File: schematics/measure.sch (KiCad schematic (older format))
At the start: 7 parts

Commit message: split into 2 sheets + drc
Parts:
- gave numbers to parts that had none: 7
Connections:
- net at U3.1 (IN+): now also P6.2 (P2), U3.12 (VBUS), U3.2 (IN+), U3.3 (IN+)
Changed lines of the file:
@@
 $EndDescr
 $Comp
-L INA260 U?
+L INA260 U3
 U 1 1 5881C68E
 P 5550 4200
-F 0 "U?" H 5650 4100 60  0000 C CNN
+F 0 "U3" H 5650 4100 60  0000 C CNN
 F 1 "INA260" V 6000 4700 60  0000 C CNN
 F 2 "" H 5550 4200 60  0001 C CNN
@@
 $EndComp
 $Comp
-L R_Small R?
+L R_Small R4
 U 1 1 5881C6C5
 P 4950 3650
-F 0 "R?" V 4850 3600 50  0000 L CNN
+F 0 "R4" V 4850 3600 50  0000 L CNN
 F 1 "0R_NP" V 4950 3600 50  0000 L CNN
 F 2 "" H 4950 3650 50  0000 C CNN
@@
 $EndComp
 $Comp
-L R_Small R?
+L R_Small R5
 U 1 1 5881C6FE
 P 4950 3750
-F 0 "R?" V 5050 3700 50  0000 L CNN
+F 0 "R5" V 5050 3700 50  0000 L CNN
 F 1 "0R" V 4950 3700 50  0000 L CNN
 F 2 "" H 4950 3750 50  0000 C CNN
@@
 $EndComp
 $Comp
-L GND #PWR?
+L GND #PWR014
 U 1 1 5881C8A1
 P 4700 3750
-F 0 "#PWR?" H 4700 3500 50  0001 C CNN
+F 0 "#PWR014" H 4700 3500 50  0001 C CNN
 F 1 "GND" H 4700 3600 50  0000 C CNN
 F 2 "" H 4700 3750 50  0000 C CNN
@@
 $EndComp
 $Comp
-L +3.3V #PWR?
+L +3.3V #PWR015
 U 1 1 5881C8BE
 P 4700 3650
-F 0 "#PWR?" H 4700 3500 50  0001 C CNN
+F 0 "#PWR015" H 4700 3500 50  0001 C CNN
 F 1 "+3.3V" H 4700 3790 50  0000 C CNN
 F 2 "" H 4700 3650 50  0000 C CNN
@@
 	4700 3750 4850 3750
 $Comp
-L R_Small R?
+L R_Small R6
 U 1 1 5881C9C3
 P 4950 4150
-F 0 "R?" V 4850 4100 50  0000 L CNN
+F 0 "R6" V 4850 4100 50  0000 L CNN
 F 1 "0R_NP" V 4950 4100 50  0000 L CNN
 F 2 "" H 4950 4150 50  0000 C CNN
@@
 $EndComp
 $Comp
-L R_Small R?
+L R_Small R7
 U 1 1 5881C9C9
 P 4950 4250
-F 0 "R?" V 5050 4200 50  0000 L CNN
+F 0 "R7" V 5050 4200 50  0000 L CNN
 F 1 "0R" V 4950 4200 50  0000 L CNN
 F 2 "" H 4950 4250 50  0000 C CNN
@@
 	5150 4250 5050 4250
 $Comp
-L GND #PWR?
+L GND #PWR016
 U 1 1 5881C9D1
 P 4700 4250
-F 0 "#PWR?" H 4700 4000 50  0001 C CNN
+F 0 "#PWR016" H 4700 4000 50  0001 C CNN
 F 1 "GND" H 4700 4100 50  0000 C CNN
 F 2 "" H 4700 4250 50  0000 C CNN
@@
 $EndComp
 $Comp
-L +3.3V #PWR?
+L +3.3V #PWR017
 U 1 1 5881C9D7
 P 4700 4150
-F 0 "#PWR?" H 4700 4000 50  0001 C CNN
+F 0 "#PWR017" H 4700 4000 50  0001 C CNN
 F 1 "+3.3V" H 4700 4290 50  0000 C CNN
 F 2 "" H 4700 4150 50  0000 C CNN
@@
 	6700 4000 6700 4100
 $Comp
-L GND #PWR?
+L GND #PWR018
 U 1 1 5881CC9E
 P 6700 4100
-F 0 "#PWR?" H 6700 3850 50  0001 C CNN
+F 0 "#PWR018" H 6700 3850 50  0001 C CNN
 F 1 "GND" H 6700 3950 50  0000 C CNN
 F 2 "" H 6700 4100 50  0000 C CNN
@@
 	6700 3900 7150 3900
 $Comp
-L +3.3V #PWR?
+L +3.3V #PWR019
 U 1 1 5881CD56
 P 7700 3850
-F 0 "#PWR?" H 7700 3700 50  0001 C CNN
+F 0 "#PWR019" H 7700 3700 50  0001 C CNN
 F 1 "+3.3V" H 7700 3990 50  0000 C CNN
 F 2 "" H 7700 3850 50  0000 C CNN
@@
 Connection ~ 6950 3900
 $Comp
-L CONN_01X02 P?
+L CONN_01X02 P7
 U 1 1 5881CF01
 P 7250 3250
-F 0 "P?" H 7250 3400 50  0000 C CNN
+F 0 "P7" H 7250 3400 50  0000 C CNN
 F 1 "Power_OUT" V 7350 3250 50  0000 C CNN
 F 2 "" H 7250 3250 50  0000 C CNN
@@
 $EndComp
 $Comp
-L CONN_01X02 P?
+L CONN_01X02 P6
 U 1 1 5881CF96
 P 4700 3150
-F 0 "P?" H 4700 3300 50  0000 C CNN
+F 0 "P6" H 4700 3300 50  0000 C CNN
 F 1 "Power_IN" V 4800 3150 50  0000 C CNN
 F 2 "" H 4700 3150 50  0000 C CNN
@@
 	6700 3200 7050 3200
 $Comp
-L GND #PWR?
+L GND #PWR020
 U 1 1 5881D061
 P 7050 3300
-F 0 "#PWR?" H 7050 3050 50  0001 C CNN
+F 0 "#PWR020" H 7050 3050 50  0001 C CNN
 F 1 "GND" H 7050 3150 50  0000 C CNN
 F 2 "" H 7050 3300 50  0000 C CNN
@@
 	5350 3100 4900 3100
 $Comp
-L GND #PWR?
+L GND #PWR021
 U 1 1 5881D145
 P 4900 3200
-F 0 "#PWR?" H 4900 2950 50  0001 C CNN
+F 0 "#PWR021" H 4900 2950 50  0001 C CNN
 F 1 "GND" H 4900 3050 50  0000 C CNN
 F 2 "" H 4900 3200 50  0000 C CNN
@@
 Wire Wire Line
 	6950 3850 7700 3850
+Connection ~ 5350 3200
+Connection ~ 6700 3400
+Connection ~ 6700 3200
 $EndSCHEMATC

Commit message: added pullups for I2C and alert
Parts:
- added R13, R14, R15: 1K, Resistors_SMD:R_0805_HandSoldering, symbol R_Small
- P6, P7: footprint (none) -> Terminal_Blocks:TerminalBlock_Pheonix_MKDS1.5-2pol
- R10: renamed from R5; footprint (none) -> Resistors_SMD:R_0805_HandSoldering
- R11: renamed from R6; footprint (none) -> Resistors_SMD:R_0805_HandSoldering
- R12: renamed from R7; footprint (none) -> Resistors_SMD:R_0805_HandSoldering
- R9: renamed from R4; footprint (none) -> Resistors_SMD:R_0805_HandSoldering
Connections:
- net +3V3: now also R13.1
- net ALERT: now also R15.2
- net I2C_SCL: now also R14.2
- net I2C_SDA: now also R13.2, R14.1, R15.1
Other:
- moved on the sheet: P7
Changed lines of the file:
@@
 $EndComp
 $Comp
-L R_Small R4
+L R_Small R9
 U 1 1 5881C6C5
 P 4950 3650
-F 0 "R4" V 4850 3600 50  0000 L CNN
+F 0 "R9" V 4850 3600 50  0000 L CNN
 F 1 "0R_NP" V 4950 3600 50  0000 L CNN
-F 2 "" H 4950 3650 50  0000 C CNN
+F 2 "Resistors_SMD:R_0805_HandSoldering" H 4950 3650 50  0001 C CNN
 F 3 "" H 4950 3650 50  0000 C CNN
 	1    4950 3650
@@
 $EndComp
 $Comp
-L R_Small R5
+L R_Small R10
 U 1 1 5881C6FE
 P 4950 3750
-F 0 "R5" V 5050 3700 50  0000 L CNN
+F 0 "R10" V 5050 3700 50  0000 L CNN
 F 1 "0R" V 4950 3700 50  0000 L CNN
-F 2 "" H 4950 3750 50  0000 C CNN
+F 2 "Resistors_SMD:R_0805_HandSoldering" H 4950 3750 50  0001 C CNN
 F 3 "" H 4950 3750 50  0000 C CNN
 	1    4950 3750
@@
 	4700 3750 4850 3750
 $Comp
-L R_Small R6
+L R_Small R11
 U 1 1 5881C9C3
 P 4950 4150
-F 0 "R6" V 4850 4100 50  0000 L CNN
+F 0 "R11" V 4850 4100 50  0000 L CNN
 F 1 "0R_NP" V 4950 4100 50  0000 L CNN
-F 2 "" H 4950 4150 50  0000 C CNN
+F 2 "Resistors_SMD:R_0805_HandSoldering" H 4950 4150 50  0001 C CNN
 F 3 "" H 4950 4150 50  0000 C CNN
 	1    4950 4150
@@
 $EndComp
 $Comp
-L R_Small R7
+L R_Small R12
 U 1 1 5881C9C9
 P 4950 4250
-F 0 "R7" V 5050 4200 50  0000 L CNN
+F 0 "R12" V 5050 4200 50  0000 L CNN
 F 1 "0R" V 4950 4200 50  0000 L CNN
-F 2 "" H 4950 4250 50  0000 C CNN
+F 2 "Resistors_SMD:R_0805_HandSoldering" H 4950 4250 50  0001 C CNN
 F 3 "" H 4950 4250 50  0000 C CNN
 	1    4950 4250
@@
 L +3.3V #PWR019
 U 1 1 5881CD56
-P 7700 3850
-F 0 "#PWR019" H 7700 3700 50  0001 C CNN
-F 1 "+3.3V" H 7700 3990 50  0000 C CNN
-F 2 "" H 7700 3850 50  0000 C CNN
-F 3 "" H 7700 3850 50  0000 C CNN
-	1    7700 3850
+P 7500 3850
+F 0 "#PWR019" H 7500 3700 50  0001 C CNN
+F 1 "+3.3V" H 7600 3850 50  0000 C CNN
+F 2 "" H 7500 3850 50  0000 C CNN
+F 3 "" H 7500 3850 50  0000 C CNN
+	1    7500 3850
 	1    0    0    -1
 $EndComp
@@
 L CONN_01X02 P7
 U 1 1 5881CF01
-P 7250 3250
-F 0 "P7" H 7250 3400 50  0000 C CNN
-F 1 "Power_OUT" V 7350 3250 50  0000 C CNN
-F 2 "" H 7250 3250 50  0000 C CNN
-F 3 "" H 7250 3250 50  0000 C CNN
-	1    7250 3250
+P 7000 3250
+F 0 "P7" H 7000 3400 50  0000 C CNN
+F 1 "Power_OUT" V 7100 3250 50  0000 C CNN
+F 2 "Terminal_Blocks:TerminalBlock_Pheonix_MKDS1.5-2pol" H 7000 3250 50  0001 C CNN
+F 3 "" H 7000 3250 50  0000 C CNN
+	1    7000 3250
 	1    0    0    -1
 $EndComp
@@
 F 0 "P6" H 4700 3300 50  0000 C CNN
 F 1 "Power_IN" V 4800 3150 50  0000 C CNN
-F 2 "" H 4700 3150 50  0000 C CNN
+F 2 "Terminal_Blocks:TerminalBlock_Pheonix_MKDS1.5-2pol" H 4700 3150 50  0001 C CNN
 F 3 "" H 4700 3150 50  0000 C CNN
 	1    4700 3150
@@
 Connection ~ 6700 3300
 Wire Wire Line
-	6700 3200 7050 3200
+	6700 3200 6800 3200
 $Comp
 L GND #PWR020
 U 1 1 5881D061
-P 7050 3300
-F 0 "#PWR020" H 7050 3050 50  0001 C CNN
-F 1 "GND" H 7050 3150 50  0000 C CNN
-F 2 "" H 7050 3300 50  0000 C CNN
-F 3 "" H 7050 3300 50  0000 C CNN
-	1    7050 3300
+P 6800 3300
+F 0 "#PWR020" H 6800 3050 50  0001 C CNN
+F 1 "GND" H 6800 3150 50  0000 C CNN
+F 2 "" H 6800 3300 50  0000 C CNN
+F 3 "" H 6800 3300 50  0000 C CNN
+	1    6800 3300
 	1    0    0    -1
 $EndComp
@@
 $EndComp
 Connection ~ 5350 3400
-Text HLabel 7150 3550 2    60   Input ~ 0
+Text HLabel 7650 3550 2    60   Input ~ 0
 I2C_SDA
-Text HLabel 7150 3650 2    60   Input ~ 0
+Text HLabel 7700 3650 2    60   Input ~ 0
 I2C_SCL
-Text HLabel 7150 3750 2    60   Input ~ 0
+Text HLabel 7750 3750 2    60   Input ~ 0
 ALERT
 Wire Wire Line
-	6700 3550 7150 3550
-Wire Wire Line
-	6700 3650 7150 3650
-Wire Wire Line
-	6700 3750 7150 3750
+	6700 3750 7750 3750
 Wire Wire Line
 	6950 3900 6950 3850
 Wire Wire Line
-	6950 3850 7700 3850
+	6950 3850 7500 3850
 Connection ~ 5350 3200
 Connection ~ 6700 3400
 Connection ~ 6700 3200
+$Comp
+L R_Small R13
+U 1 1 58841DD5
+P 7250 3100
+F 0 "R13" H 7280 3120 50  0000 L CNN
+F 1 "1K" H 7280 3060 50  0000 L CNN
+F 2 "Resistors_SMD:R_0805_HandSoldering" H 7250 3100 50  0001 C CNN
+F 3 "" H 7250 3100 50  0000 C CNN
+	1    7250 3100
+	1    0    0    -1
+$EndComp
+$Comp
+L R_Small R14
+U 1 1 58841E1B
+P 7400 3300
+F 0 "R14" H 7430 3320 50  0000 L CNN
+F 1 "1K" H 7430 3260 50  0000 L CNN
+F 2 "Resistors_SMD:R_0805_HandSoldering" H 7400 3300 50  0001 C CNN
+F 3 "" H 7400 3300 50  0000 C CNN
+	1    7400 3300
+	1    0    0    -1
+$EndComp
+$Comp
+L R_Small R15
+U 1 1 58841E6E
+P 7600 3400
+F 0 "R15" H 7630 3420 50  0000 L CNN
+F 1 "1K" H 7630 3360 50  0000 L CNN
+F 2 "Resistors_SMD:R_0805_HandSoldering" H 7600 3400 50  0001 C CNN
+F 3 "" H 7600 3400 50  0000 C CNN
+	1    7600 3400
+	1    0    0    -1
+$EndComp
+Wire Wire Line
+	7250 3200 7250 3550
+Wire Wire Line
+	7250 3200 7600 3200
+$Comp
+L +3.3V #PWR022
+U 1 1 58841F37
+P 7250 3000
+F 0 "#PWR022" H 7250 2850 50  0001 C CNN
+F 1 "+3.3V" H 7250 3140 50  0000 C CNN
+F 2 "" H 7250 3000 50  0000 C CNN
+F 3 "" H 7250 3000 50  0000 C CNN
+	1    7250 3000
+	1    0    0    -1
+$EndComp
+Wire Wire Line
+	7600 3500 7600 3750
+Connection ~ 7600 3750
+Wire Wire Line
+	6700 3650 7700 3650
+Wire Wire Line
+	6700 3550 7650 3550
+Wire Wire Line
+	7400 3400 7400 3650
+Connection ~ 7400 3650
+Connection ~ 7250 3550
+Wire Wire Line
+	7600 3200 7600 3300
+Connection ~ 7400 3200
 $EndSCHEMATC

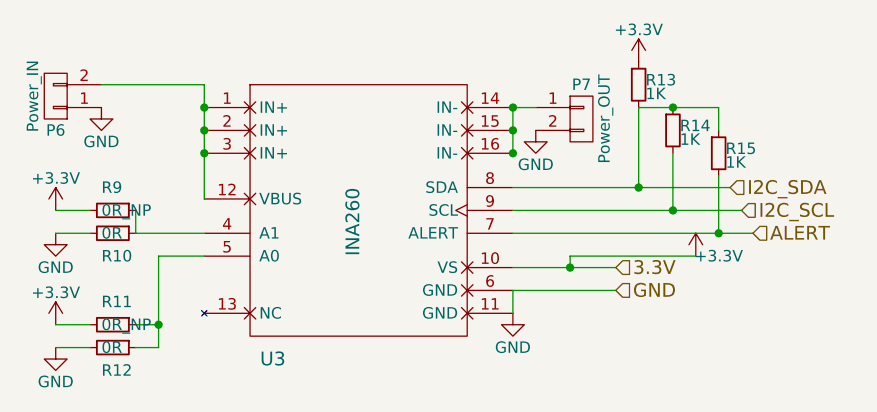
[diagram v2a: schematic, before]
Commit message: added moar decoulping caps
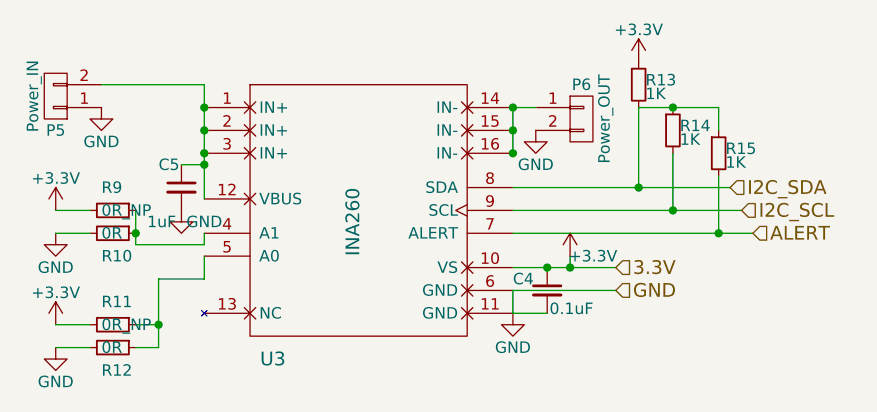
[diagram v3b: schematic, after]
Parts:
- added C4: 0.1uF, Capacitors_SMD:C_0805_HandSoldering, symbol C_Small
- added C5: 1uF, Capacitors_SMD:C_0805_HandSoldering, symbol C_Small
- renumbered P6 to P5, P7 to P6
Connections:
- net +3V3: now also C4.1
- net GND: now also C4.2, C5.2
- net at P5.2 (P2), U3.1 (IN+), U3.12 (VBUS)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: now also C5.1
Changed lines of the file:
@@
 	4700 4250 4850 4250
 Wire Wire Line
-	5050 3650 5050 3750
-Wire Wire Line
-	5050 3750 5350 3750
-Wire Wire Line
-	5150 3850 5150 4250
-Wire Wire Line
-	5150 3850 5350 3850
-Connection ~ 5150 4150
+	5050 3650 5050 3800
+Wire Wire Line
+	5150 3950 5150 4250
 Wire Wire Line
 	6700 4000 6700 4100
@@
 L +3.3V #PWR019
 U 1 1 5881CD56
-P 7500 3850
-F 0 "#PWR019" H 7500 3700 50  0001 C CNN
-F 1 "+3.3V" H 7600 3850 50  0000 C CNN
-F 2 "" H 7500 3850 50  0000 C CNN
-F 3 "" H 7500 3850 50  0000 C CNN
-	1    7500 3850
+P 6950 3850
+F 0 "#PWR019" H 6950 3700 50  0001 C CNN
+F 1 "+3.3V" H 7050 3850 50  0000 C CNN
+F 2 "" H 6950 3850 50  0000 C CNN
+F 3 "" H 6950 3850 50  0000 C CNN
+	1    6950 3850
 	1    0    0    -1
 $EndComp
 Connection ~ 6950 3900
 $Comp
-L CONN_01X02 P7
+L CONN_01X02 P6
 U 1 1 5881CF01
 P 7000 3250
-F 0 "P7" H 7000 3400 50  0000 C CNN
+F 0 "P6" H 7000 3400 50  0000 C CNN
 F 1 "Power_OUT" V 7100 3250 50  0000 C CNN
 F 2 "Terminal_Blocks:TerminalBlock_Pheonix_MKDS1.5-2pol" H 7000 3250 50  0001 C CNN
@@
 $EndComp
 $Comp
-L CONN_01X02 P6
+L CONN_01X02 P5
 U 1 1 5881CF96
 P 4700 3150
-F 0 "P6" H 4700 3300 50  0000 C CNN
+F 0 "P5" H 4700 3300 50  0000 C CNN
 F 1 "Power_IN" V 4800 3150 50  0000 C CNN
 F 2 "Terminal_Blocks:TerminalBlock_Pheonix_MKDS1.5-2pol" H 4700 3150 50  0001 C CNN
@@
 	6700 3750 7750 3750
 Wire Wire Line
-	6950 3900 6950 3850
-Wire Wire Line
-	6950 3850 7500 3850
+	6950 3850 6950 3900
 Connection ~ 5350 3200
 Connection ~ 6700 3400
@@
 	7600 3200 7600 3300
 Connection ~ 7400 3200
+$Comp
+L C_Small C4
+U 1 1 58842FC4
+P 6850 4000
+F 0 "C4" H 6700 4050 50  0000 L CNN
+F 1 "0.1uF" H 6860 3920 50  0000 L CNN
+F 2 "Capacitors_SMD:C_0805_HandSoldering" H 6850 4000 50  0001 C CNN
+F 3 "" H 6850 4000 50  0000 C CNN
+	1    6850 4000
+	1    0    0    -1
+$EndComp
+Wire Wire Line
+	6700 4100 6850 4100
+Connection ~ 6850 3900
+$Comp
+L C_Small C5
+U 1 1 58847B1B
+P 5250 3550
+F 0 "C5" H 5150 3650 50  0000 L CNN
+F 1 "1uF" H 5100 3400 50  0000 L CNN
+F 2 "Capacitors_SMD:C_0805_HandSoldering" H 5250 3550 50  0001 C CNN
+F 3 "" H 5250 3550 50  0000 C CNN
+	1    5250 3550
+	1    0    0    -1
+$EndComp
+Wire Wire Line
+	5250 3450 5350 3450
+Connection ~ 5350 3450
+$Comp
+L GND #PWR023
+U 1 1 58847CCB
+P 5250 3650
+F 0 "#PWR023" H 5250 3400 50  0001 C CNN
+F 1 "GND" H 5350 3600 50  0000 C CNN
+F 2 "" H 5250 3650 50  0000 C CNN
+F 3 "" H 5250 3650 50  0000 C CNN
+	1    5250 3650
+	1    0    0    -1
+$EndComp
+Wire Wire Line
+	5350 3750 5350 3800
+Wire Wire Line
+	5350 3800 5050 3800
+Connection ~ 5050 3750
+Wire Wire Line
+	5350 3850 5350 3950
+Wire Wire Line
+	5350 3950 5150 3950
+Connection ~ 5150 4150
 $EndSCHEMATC

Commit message: added footprint for switch
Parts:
- U3: footprint (none) -> Housings_SSOP:TSSOP-16_4.4x5mm_Pitch0.65mm
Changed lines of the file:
@@
 F 0 "U3" H 5650 4100 60  0000 C CNN
 F 1 "INA260" V 6000 4700 60  0000 C CNN
-F 2 "" H 5550 4200 60  0001 C CNN
+F 2 "Housings_SSOP:TSSOP-16_4.4x5mm_Pitch0.65mm" H 5550 4200 60  0001 C CNN
 F 3 "" H 5550 4200 60  0001 C CNN
 	1    5550 4200
